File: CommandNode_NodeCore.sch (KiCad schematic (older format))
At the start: 1 part

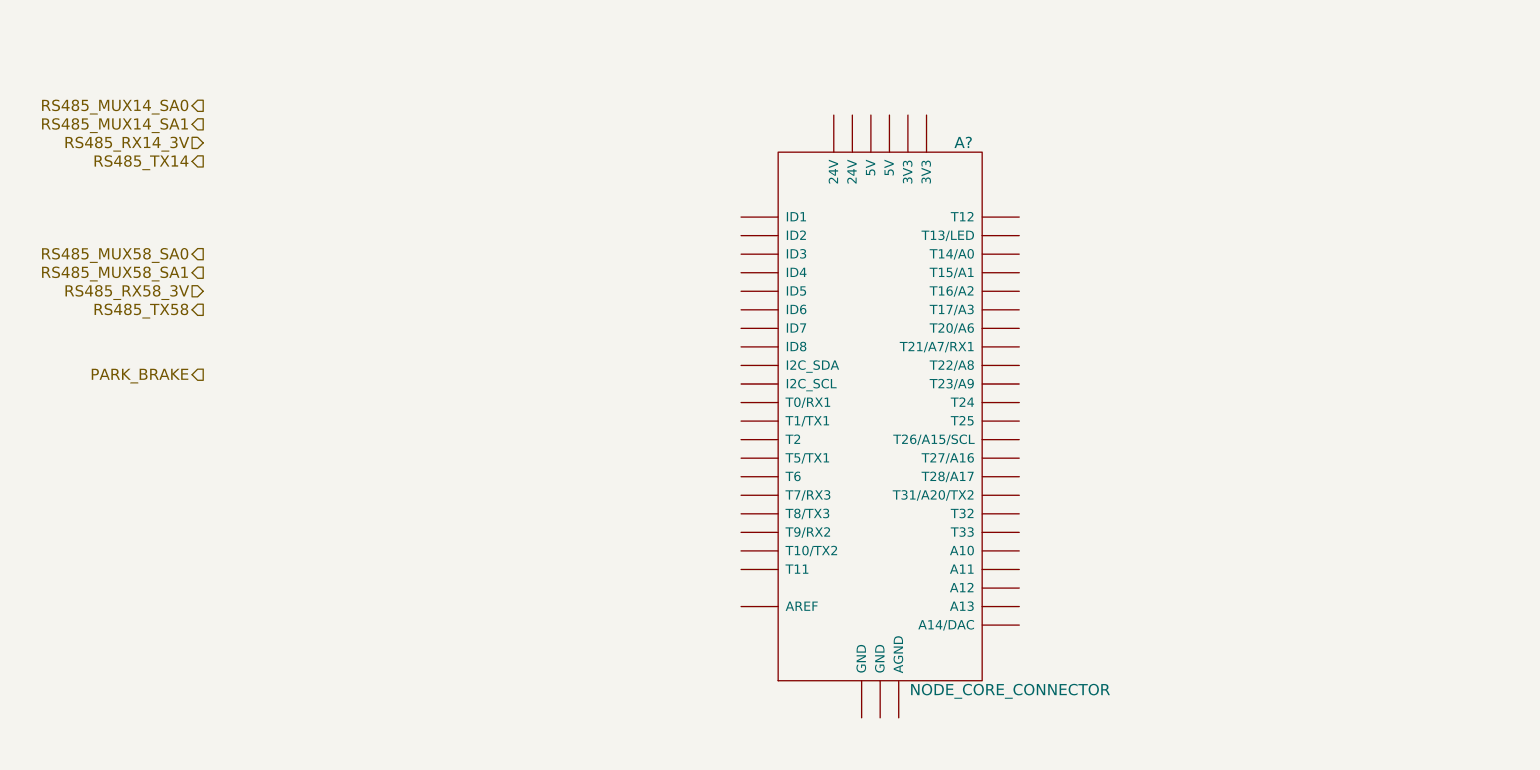
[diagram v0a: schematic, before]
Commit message: Update charger control interface
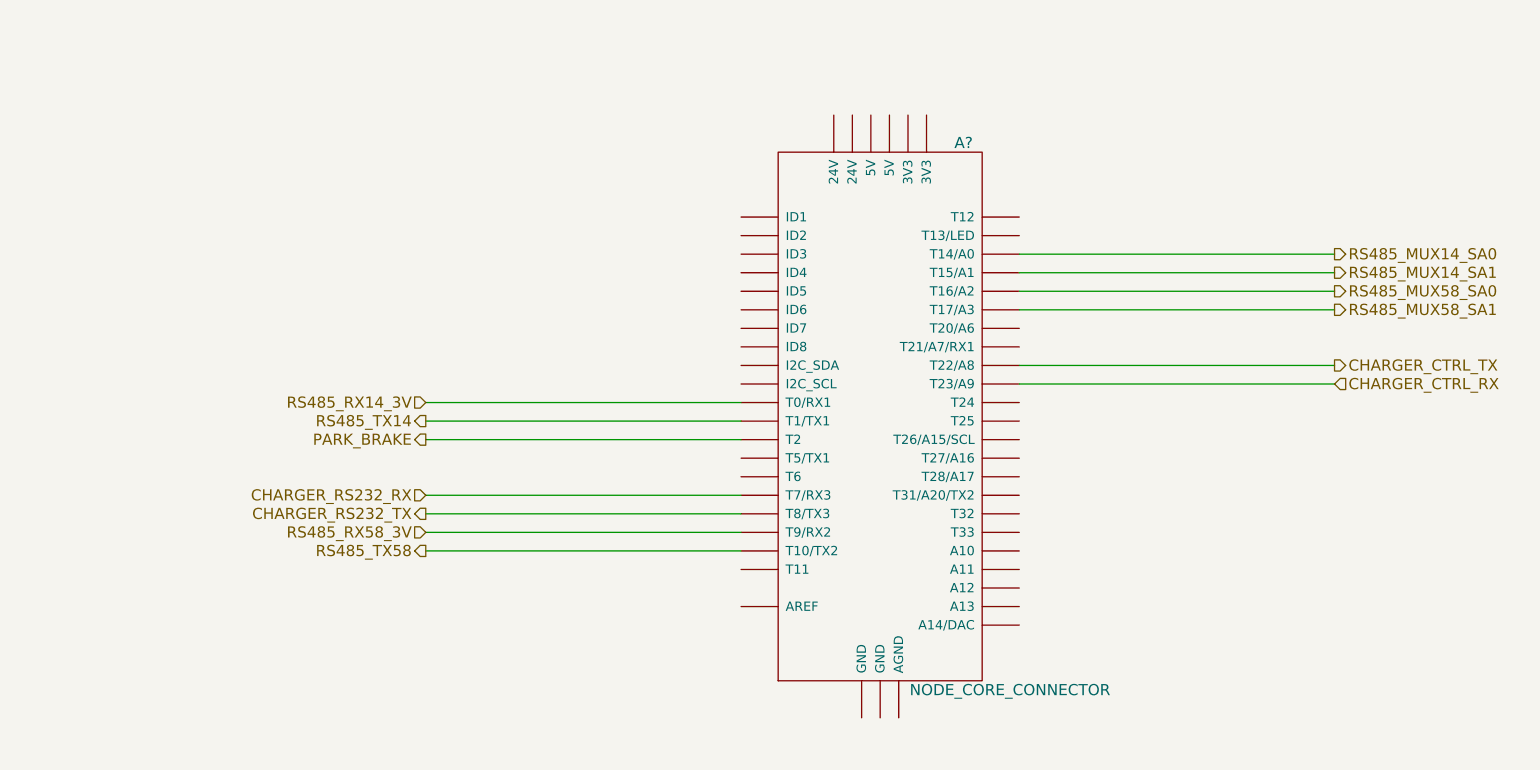
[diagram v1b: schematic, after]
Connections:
- net PARK_BRAKE: now also A?.T2
- net RS485_MUX14_SA0: now also A?.T14 (T14/A0)
- net RS485_MUX14_SA1: now also A?.T15 (T15/A1)
- net RS485_MUX58_SA0: now also A?.T16 (T16/A2)
- net RS485_MUX58_SA1: now also A?.T17 (T17/A3)
- net RS485_RX14_3V: now also A?.T0 (T0/RX1)
- net RS485_RX58_3V: now also A?.T9 (T9/RX2)
- net RS485_TX14: now also A?.T1 (T1/TX1)
- net RS485_TX58: now also A?.T10 (T10/TX2)
- net CHARGER_CTRL_TX: now reaches A?.T22 (T22/A8)
- net CHARGER_CTRL_RX: now reaches A?.T23 (T23/A9)
- net CHARGER_RS232_RX: now reaches A?.T7 (T7/RX3)
- net CHARGER_RS232_TX: now reaches A?.T8 (T8/TX3)
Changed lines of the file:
@@
 Comment4 ""
 $EndDescr
-Text HLabel 1900 2000 0    60   Output ~ 0
+Text HLabel 8000 2800 2    60   Output ~ 0
 RS485_MUX14_SA0
-Text HLabel 1900 2100 0    60   Output ~ 0
+Text HLabel 8000 2900 2    60   Output ~ 0
 RS485_MUX14_SA1
-Text HLabel 1900 2300 0    60   Output ~ 0
+Text HLabel 3100 3700 0    60   Output ~ 0
 RS485_TX14
-Text HLabel 1900 2200 0    60   Input ~ 0
+Text HLabel 3100 3600 0    60   Input ~ 0
 RS485_RX14_3V
-Text HLabel 1900 2800 0    60   Output ~ 0
+Text HLabel 8000 3000 2    60   Output ~ 0
 RS485_MUX58_SA0
-Text HLabel 1900 2900 0    60   Output ~ 0
+Text HLabel 8000 3100 2    60   Output ~ 0
 RS485_MUX58_SA1
-Text HLabel 1900 3100 0    60   Output ~ 0
+Text HLabel 3100 4400 0    60   Output ~ 0
 RS485_TX58
-Text HLabel 1900 3000 0    60   Input ~ 0
+Text HLabel 3100 4300 0    60   Input ~ 0
 RS485_RX58_3V
 $Comp
@@
 	1    0    0    -1
 $EndComp
-Text HLabel 1900 3450 0    60   Output ~ 0
+Text HLabel 3100 3800 0    60   Output ~ 0
 PARK_BRAKE
+Wire Wire Line
+	4800 3600 3100 3600
+Wire Wire Line
+	4800 3700 3100 3700
+Wire Wire Line
+	4800 4100 3100 4100
+Wire Wire Line
+	4800 4200 3100 4200
+Wire Wire Line
+	4800 4300 3100 4300
+Wire Wire Line
+	4800 4400 3100 4400
+Wire Wire Line
+	8000 2800 6300 2800
+Wire Wire Line
+	8000 2900 6300 2900
+Wire Wire Line
+	8000 3000 6300 3000
+Wire Wire Line
+	8000 3100 6300 3100
+Wire Wire Line
+	4800 3800 3100 3800
+Text HLabel 8000 3400 2    60   Output ~ 0
+CHARGER_CTRL_TX
+Text HLabel 3100 4100 0    60   Input ~ 0
+CHARGER_RS232_RX
+Text HLabel 8000 3500 2    60   Input ~ 0
+CHARGER_CTRL_RX
+Text HLabel 3100 4200 0    60   Output ~ 0
+CHARGER_RS232_TX
+Wire Wire Line
+	8000 3400 6300 3400
+Wire Wire Line
+	8000 3500 6300 3500
 $EndSCHEMATC

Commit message: Finish and print schematics for review
Lifting mechanism, charger interface, Data Enable on HE controller
RS585, Park Brake and node core.
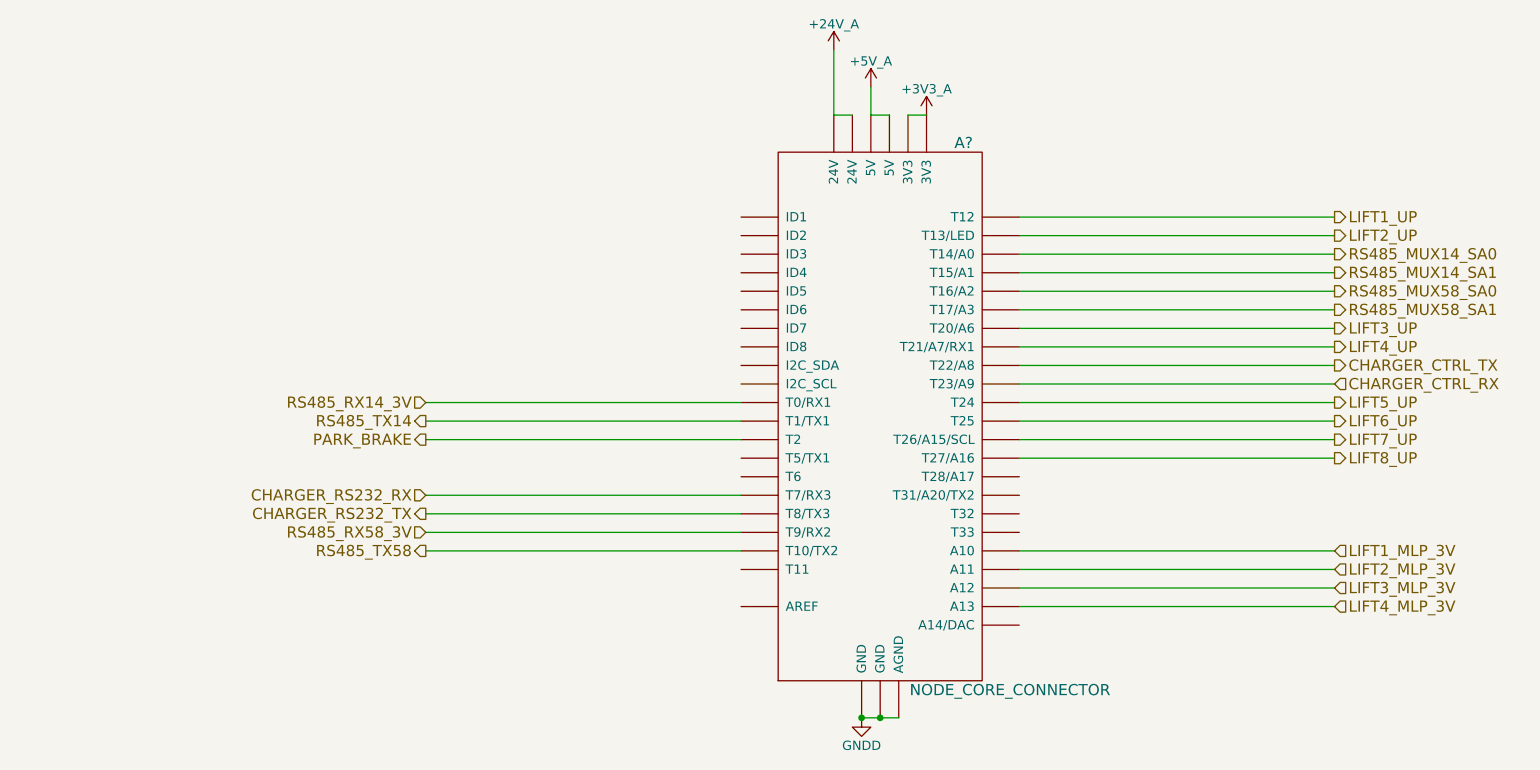
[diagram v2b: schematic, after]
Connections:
- net +5V: now reaches A?.+24V (24V)
- net +5V: now also A?.+5V (5V)
- net +3V3: now reaches A?.+3V3 (3V3)
- net LIFT1_MLP_3V: now reaches A?.A10
- net LIFT2_MLP_3V: now reaches A?.A11
- net LIFT3_MLP_3V: now reaches A?.A12
- net LIFT4_MLP_3V: now reaches A?.A13
- net GNDD: now reaches A?.AGND
- net GNDD: now also A?.GND
- net LIFT1_UP: now reaches A?.T12
- net LIFT2_UP: now reaches A?.T13 (T13/LED)
- net LIFT3_UP: now reaches A?.T20 (T20/A6)
- net LIFT4_UP: now reaches A?.T21 (T21/A7/RX1)
- net LIFT5_UP: now reaches A?.T24
- net LIFT6_UP: now reaches A?.T25
- net LIFT7_UP: now reaches A?.T26 (T26/A15/SCL)
- net LIFT8_UP: now reaches A?.T27 (T27/A16)
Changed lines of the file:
@@
 $Descr A3 16535 11693
 encoding utf-8
-Sheet 6 7
+Sheet 6 8
 Title "Node Core Interface"
 Date ""
@@
 Wire Wire Line
 	8000 3500 6300 3500
+$Comp
+L +24V_A #PWR?
+U 1 1 576A35E4
+P 5300 1700
+F 0 "#PWR?" H 5300 1550 50  0001 C CNN
+F 1 "+24V_A" H 5300 1840 50  0000 C CNN
+F 2 "" H 5300 1700 60  0000 C CNN
+F 3 "" H 5300 1700 60  0000 C CNN
+	1    5300 1700
+	1    0    0    -1
+$EndComp
+$Comp
+L +5V_A #PWR?
+U 1 1 576A35FA
+P 5500 1900
+F 0 "#PWR?" H 5500 1750 50  0001 C CNN
+F 1 "+5V_A" H 5500 2040 50  0000 C CNN
+F 2 "" H 5500 1900 60  0000 C CNN
+F 3 "" H 5500 1900 60  0000 C CNN
+	1    5500 1900
+	1    0    0    -1
+$EndComp
+$Comp
+L +3V3_A #PWR?
+U 1 1 576A3610
+P 5800 2050
+F 0 "#PWR?" H 5800 1900 50  0001 C CNN
+F 1 "+3V3_A" H 5800 2190 50  0000 C CNN
+F 2 "" H 5800 2050 60  0000 C CNN
+F 3 "" H 5800 2050 60  0000 C CNN
+	1    5800 2050
+	1    0    0    -1
+$EndComp
+Wire Wire Line
+	5300 1700 5300 2050
+Wire Wire Line
+	5300 2050 5400 2050
+Wire Wire Line
+	5500 1900 5500 2050
+Wire Wire Line
+	5500 2050 5600 2050
+Wire Wire Line
+	5700 2050 5800 2050
+$Comp
+L GNDD #PWR?
+U 1 1 576A36C0
+P 5450 5300
+F 0 "#PWR?" H 5450 5050 50  0001 C CNN
+F 1 "GNDD" H 5450 5150 50  0000 C CNN
+F 2 "" H 5450 5300 50  0000 C CNN
+F 3 "" H 5450 5300 50  0000 C CNN
+	1    5450 5300
+	1    0    0    -1
+$EndComp
+Wire Wire Line
+	5450 5300 5650 5300
+Connection ~ 5550 5300
+Connection ~ 5450 5300
+Wire Wire Line
+	8000 2600 6300 2600
+Wire Wire Line
+	8000 2700 6300 2700
+Text HLabel 8000 2600 2    60   Output ~ 0
+LIFT1_UP
+Text HLabel 8000 2700 2    60   Output ~ 0
+LIFT2_UP
+Wire Wire Line
+	8000 3200 6300 3200
+Wire Wire Line
+	8000 3300 6300 3300
+Text HLabel 8000 3200 2    60   Output ~ 0
+LIFT3_UP
+Text HLabel 8000 3300 2    60   Output ~ 0
+LIFT4_UP
+Wire Wire Line
+	8000 3600 6300 3600
+Wire Wire Line
+	8000 3700 6300 3700
+Text HLabel 8000 3600 2    60   Output ~ 0
+LIFT5_UP
+Text HLabel 8000 3700 2    60   Output ~ 0
+LIFT6_UP
+Wire Wire Line
+	8000 3800 6300 3800
+Wire Wire Line
+	8000 3900 6300 3900
+Text HLabel 8000 3800 2    60   Output ~ 0
+LIFT7_UP
+Text HLabel 8000 3900 2    60   Output ~ 0
+LIFT8_UP
+Wire Wire Line
+	8000 4400 6300 4400
+Wire Wire Line
+	8000 4500 6300 4500
+Wire Wire Line
+	8000 4600 6300 4600
+Wire Wire Line
+	8000 4700 6300 4700
+Text HLabel 8000 4400 2    60   Input ~ 0
+LIFT1_MLP_3V
+Text HLabel 8000 4500 2    60   Input ~ 0
+LIFT2_MLP_3V
+Text HLabel 8000 4600 2    60   Input ~ 0
+LIFT3_MLP_3V
+Text HLabel 8000 4700 2    60   Input ~ 0
+LIFT4_MLP_3V
 $EndSCHEMATC
